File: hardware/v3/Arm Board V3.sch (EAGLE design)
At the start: 83 parts, among them CN1 1X4-BIG, IC1 L6208D, IC10 74LVC1G125DCK, IC2 L6208D, IC3 L6208D, IC4 LMV358IDGKR, IC5 NCP1117ST33T3G -3V3, IC6 ATMEGA16U2-MU, Q2 BC847BSMD, T1 FDN340P, T2 FDN340P, T3 FDN340P, U2 ST3485EBDR, U3 ATSAM3X8EA-AU, Y1 12MHz KX-7 20pF, Y2 32.768Khz, Y4 12MHz KX-7 20pF

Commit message: XBEE
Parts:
- added U$1: XBEE-1B2, SparkFun-RF:XBEE-1B2

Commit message: stuff
Expanded the board
Binded EA pin to PWMs
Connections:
- net PWM5: now also IC2.EN_B
- net PWM6: now also IC2.EN_A
- net PWM7: now also IC3.EN_A
- net PWM8: now also IC1.EN_A
- net PWM9: now also IC1.EN_B
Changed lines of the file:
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@@
+</segment>
+</net>
+<net name="PWM9" class="0">
+<segment>
+<pinref part="IC1" gate="G$1" pin="EN_B"/>
+<wire x1="43.18" y1="17.78" x2="45.72" y2="17.78" width="0.1524" layer="91"/>
+<label x="45.72" y="17.78" size="1.778" layer="95"/>
+</segment>
+</net>
+<net name="PWM8" class="0">
+<segment>
+<pinref part="IC1" gate="G$1" pin="EN_A"/>
+<wire x1="43.18" y1="40.64" x2="45.72" y2="40.64" width="0.1524" layer="91"/>
+<label x="45.72" y="40.64" size="1.778" layer="95"/>
+</segment>
+</net>
+<net name="PWM6" class="0">
+<segment>
+<pinref part="IC2" gate="G$1" pin="EN_A"/>
+<wire x1="106.68" y1="40.64" x2="109.22" y2="40.64" width="0.1524" layer="91"/>
+<label x="109.22" y="40.64" size="1.778" layer="95"/>
+</segment>
+</net>
+<net name="PWM5" class="0">
+<segment>
+<pinref part="IC2" gate="G$1" pin="EN_B"/>
+<wire x1="106.68" y1="17.78" x2="109.22" y2="17.78" width="0.1524" layer="91"/>
+<label x="109.22" y="17.78" size="1.778" layer="95"/>
+</segment>
+</net>
+<net name="PWM7" class="0">
+<segment>
+<pinref part="IC3" gate="G$1" pin="EN_A"/>
+<wire x1="175.26" y1="40.64" x2="177.8" y2="40.64" width="0.1524" layer="91"/>
+<label x="177.8" y="40.64" size="1.778" layer="95"/>
 </segment>
 </net>

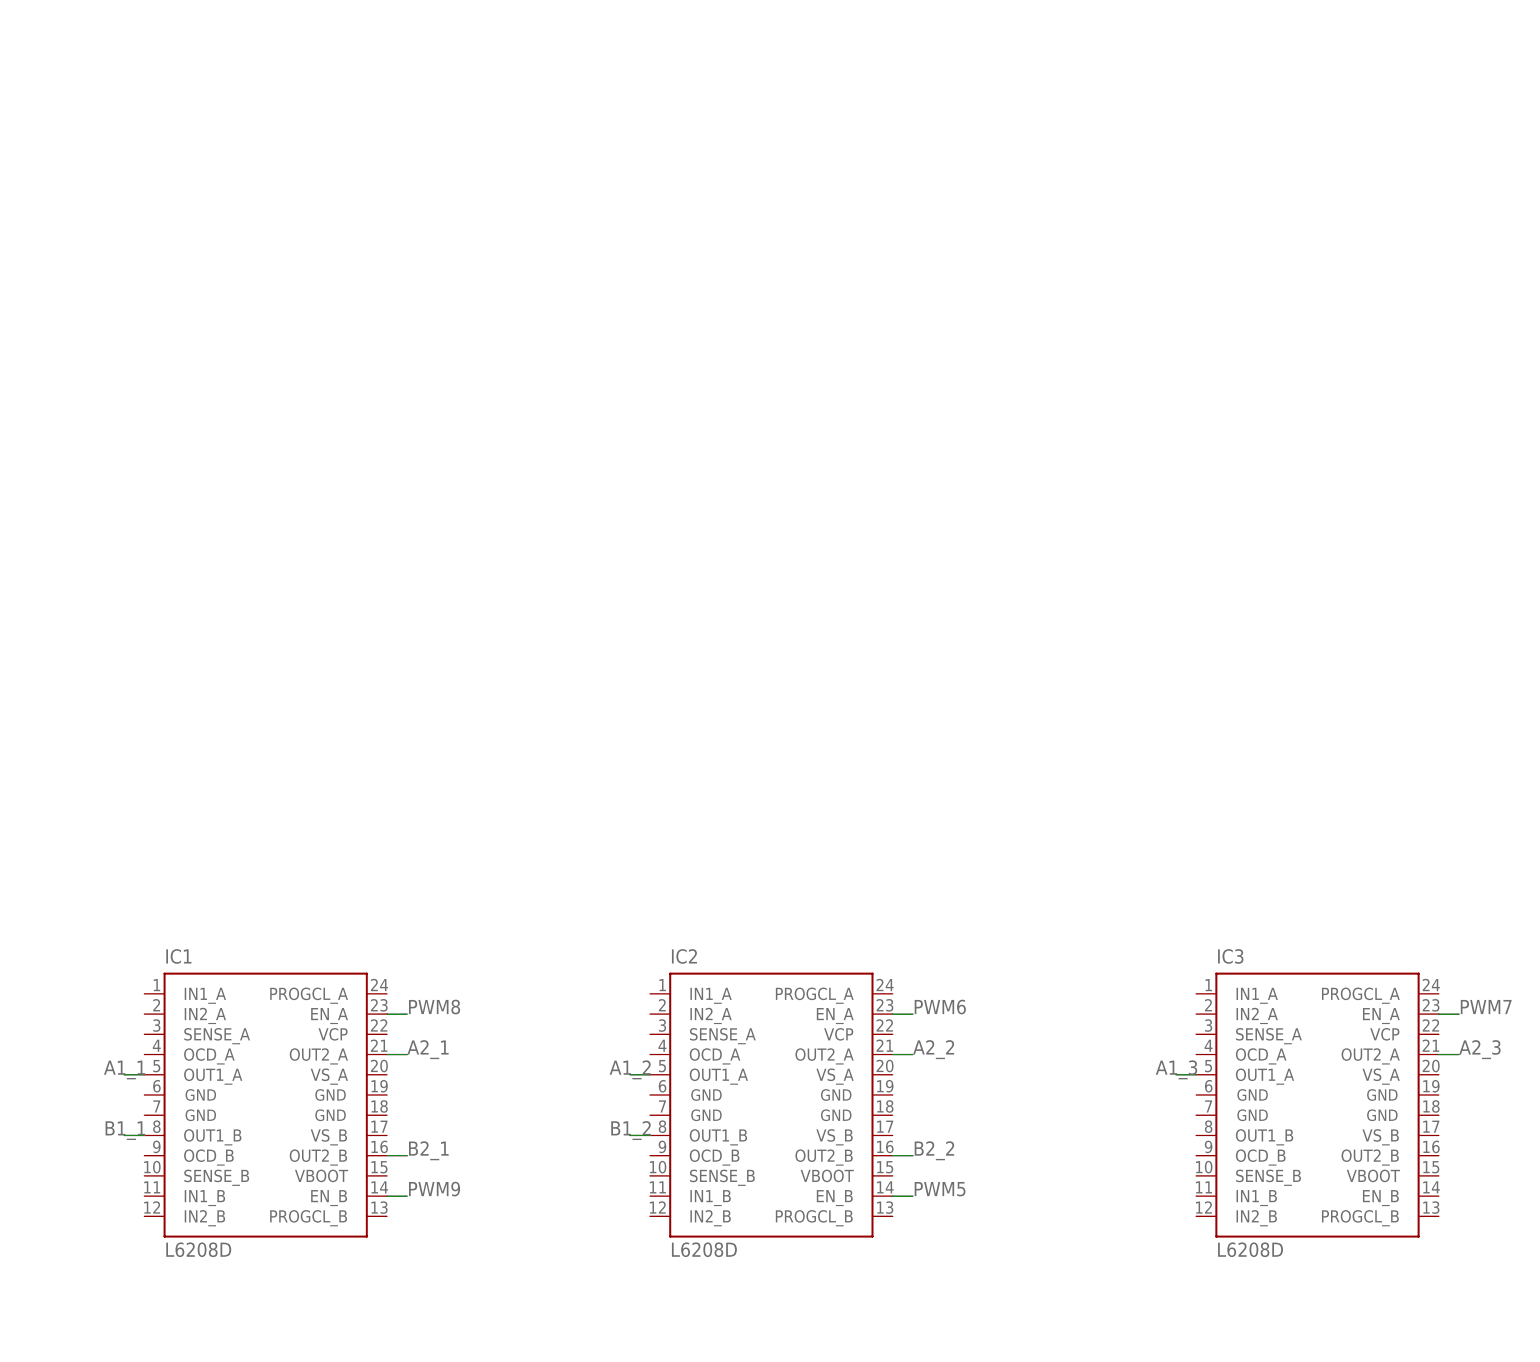
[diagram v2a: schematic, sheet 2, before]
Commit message: Connected motor controllers and Dynamixel
Bunch of stuff in the schematic
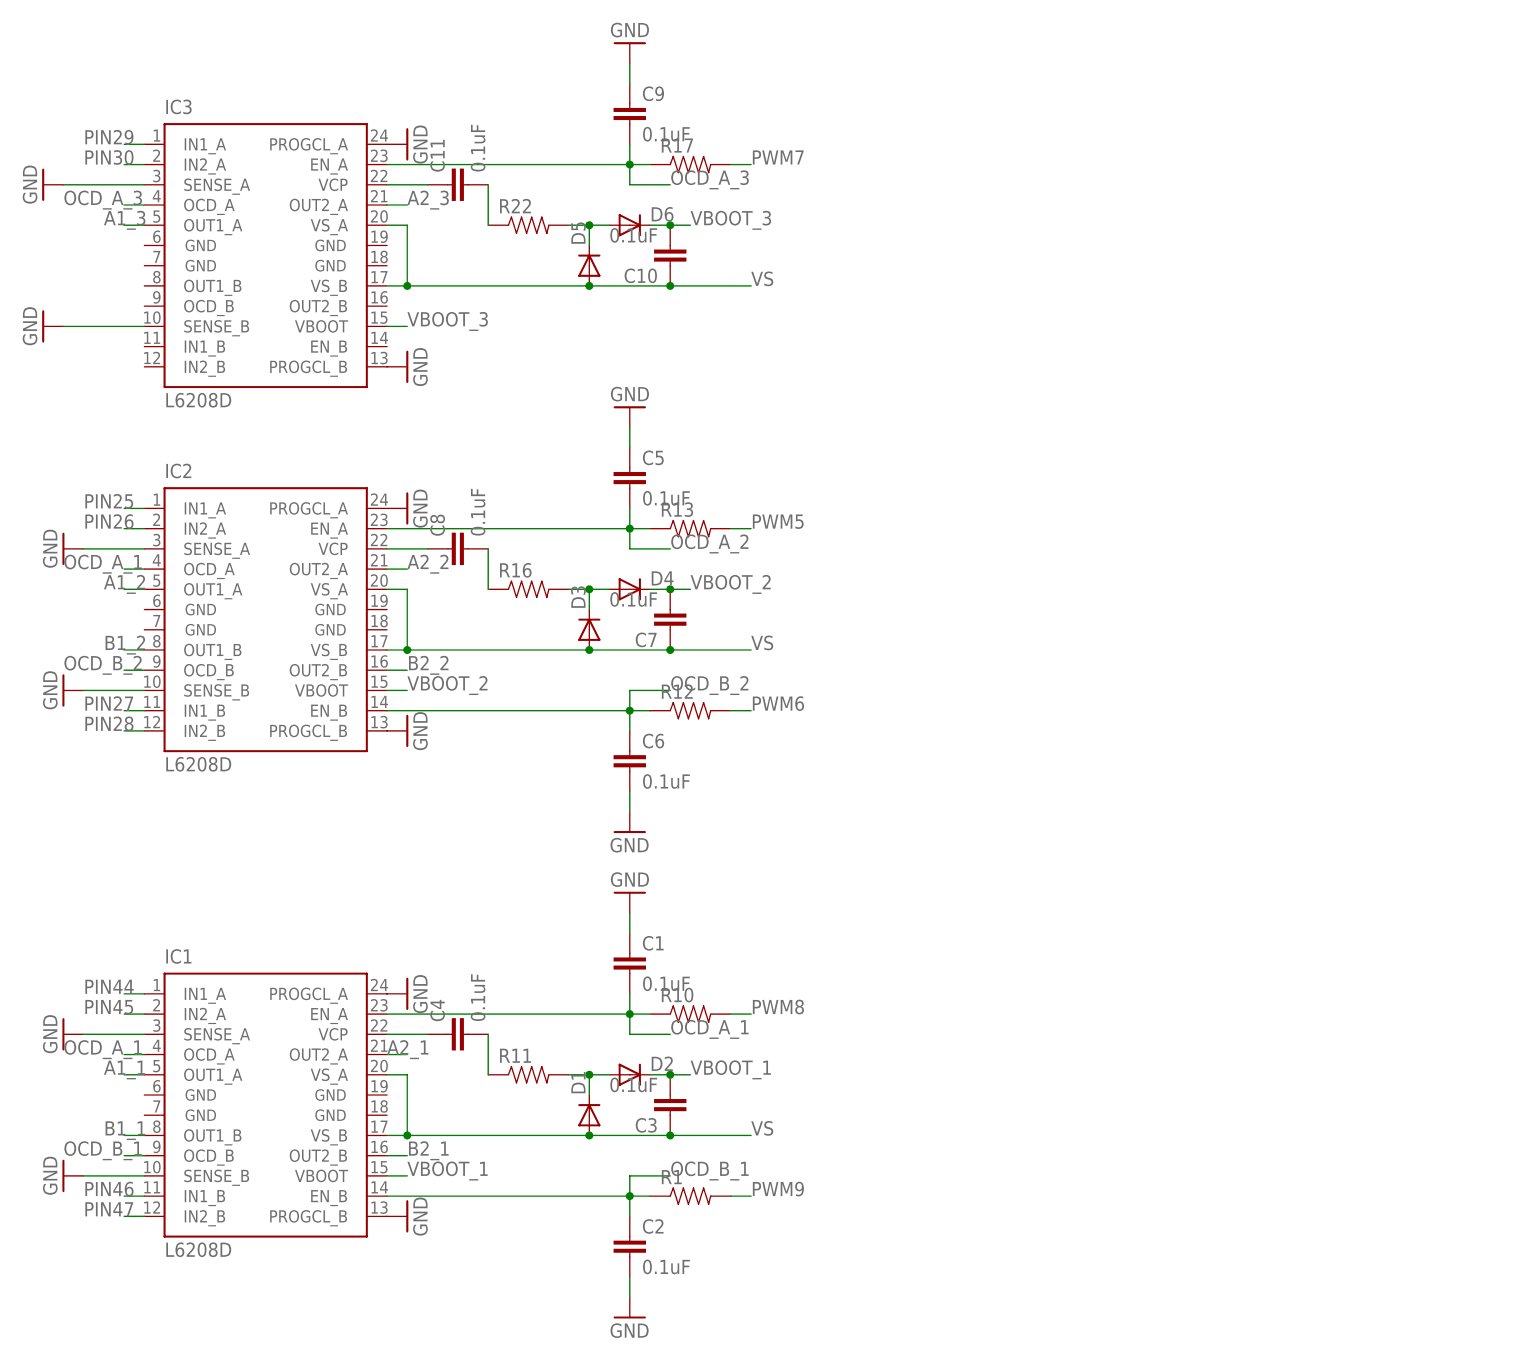
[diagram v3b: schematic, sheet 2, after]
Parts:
- removed C29: 10u, rcl:CPOL-EUSMCB
- removed C30: 100n, SmartPrj:C-EUC0402
- removed IC5: NCP1117ST33T3G -3V3, linear:MC33269ST-3.3T3
- added C1, C2, C5, C6, C9: 0.1uF, SparkFun-Capacitors:0.1UF-25V(+80/-20%)(0603)
- added C10, C11, C3, C4, C7, C8: 0.1uF, SparkFun-Capacitors:0.1UF-25V-5%(0603)
- added D1, D2, D3, D4, D5, D6: (no value), SparkFun-DiscreteSemi:DIODE1N4148
- added R1, R10, R11, R12, R13, R16, R17, R22: (no value), SparkFun-Passives:RESISTOR0805-RES
- added R24: 220, SparkFun-Passives:RESISTOR0805-RES
- U2: value ST3485EBDR -> MAX3468CSA; device ST Microelctronics_By_element14_Batch_1:ST3485EBDR -> maxim:MAX3468CSA
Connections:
- new net +12V: CN1.2
- new net DD+: CN1.3, R24.2, U2.B
- new net DD-: CN1.4, R24.1, U2.A
- new net N$10: C8.2, R16.1
- new net N$13: C4.1, IC1.VCP
- new net N$15: C4.2, R11.1
- new net N$16: C8.1, IC2.VCP
- new net N$17: D5.C, D6.A, R22.2
- new net N$18: C11.2, R22.1
- new net N$19: C11.1, IC3.VCP
- new net N$8: D3.C, D4.A, R16.2
- new net N$9: D1.C, D2.A, R11.2
- new net OCD_A_1: C1.2, IC1.EN_A, IC1.OCD_A, IC2.OCD_A, R10.1
- new net OCD_A_2: C5.2, IC2.EN_A, R13.1
- new net OCD_A_3: C9.2, IC3.EN_A, IC3.OCD_A, R17.1
- new net OCD_B_1: C2.1, IC1.EN_B, IC1.OCD_B, R1.1
- new net OCD_B_2: C6.1, IC2.EN_B, IC2.OCD_B, R12.1
- new net VBOOT_1: C3.2, D2.C, IC1.VBOOT
- new net VBOOT_2: C7.2, D4.C, IC2.VBOOT
- new net VBOOT_3: C10.2, D6.C, IC3.VBOOT
- new net VS: C10.1, C3.1, C7.1, D1.A, D3.A, D5.A, IC1.VS_A, IC1.VS_B, IC2.VS_A, IC2.VS_B, IC3.VS_A, IC3.VS_B
- net +3V3: no longer C29.+, IC5.OUT, IC5.OUT@1
- net +5V: now also U2.VCC; no longer C30.2, IC4P.V+, IC5.IN
- net GND: now also C1.1, C2.2, C5.1, C6.2, C9.1, CN1.1, IC1.PROGCL_A, IC1.PROGCL_B, IC1.SENSE_A, IC1.SENSE_B, IC2.PROGCL_A, IC2.PROGCL_B, IC2.SENSE_A, IC2.SENSE_B, IC3.PROGCL_A, IC3.PROGCL_B, IC3.SENSE_A, IC3.SENSE_B, U2.GND; no longer C29.-, C30.1, IC4P.V-, IC5.GND/ADJ
- net PIN23: now also U2.DE, U2.RE/
- net PIN25: now also IC2.IN1_A
- net PIN26: now also IC2.IN2_A
- net PIN27: now also IC2.IN1_B
- net PIN28: now also IC2.IN2_B
- net PIN29: now also IC3.IN1_A
- net PIN30: now also IC3.IN2_A
- net PIN44: now also IC1.IN1_A
- net PIN45: now also IC1.IN2_A
- net PIN46: now also IC1.IN1_B
- net PIN47: now also IC1.IN2_B
- net PWM5: now also R13.2; no longer IC2.EN_B
- net PWM6: now also R12.2; no longer IC2.EN_A
- net PWM7: now also R17.2; no longer IC3.EN_A
- net PWM8: now also R10.2; no longer IC1.EN_A
- net PWM9: now also R1.2; no longer IC1.EN_B
- net RXD1: now also U2.RO
- net TXD1: now also U2.DI
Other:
- moved on the sheet: CN1, IC2, IC3

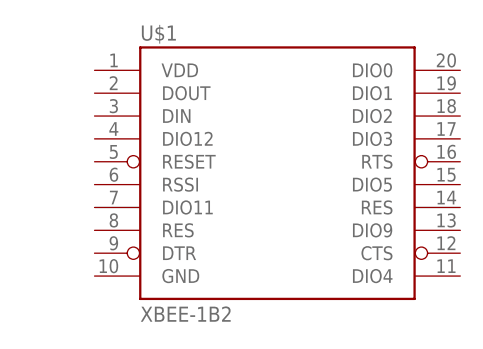
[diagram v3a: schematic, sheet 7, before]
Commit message: Added Xbee connections to schematic
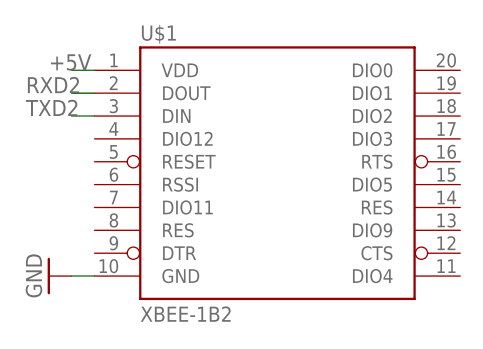
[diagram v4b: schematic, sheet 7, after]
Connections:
- net +5V: now also U$1.VDD
- net GND: now also U$1.GND
- net RXD2: now also U$1.DOUT
- net TXD2: now also U$1.DIN
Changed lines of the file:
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@@
 <part name="GND54" library="SparkFun-Aesthetics" deviceset="GND" device=""/>
 <part name="R24" library="SparkFun-Passives" deviceset="RESISTOR" device="0805-RES" value="220"/>
+<part name="GND16" library="SparkFun-Aesthetics" deviceset="GND" device=""/>
 </parts>
 <sheets>
@@
 <instances>
 <instance part="U$1" gate="G$1" x="43.18" y="35.56"/>
+<instance part="GND16" gate="1" x="17.78" y="22.86" rot="R270"/>
 </instances>
 <busses>
 </busses>
 <nets>
+<net name="+5V" class="0">
+<segment>
+<pinref part="U$1" gate="G$1" pin="VDD"/>
+<wire x1="22.86" y1="45.72" x2="20.32" y2="45.72" width="0.1524" layer="91"/>
+<label x="17.78" y="45.72" size="1.778" layer="95"/>
+</segment>
+</net>
+<net name="TXD2" class="0">
+<segment>
+<pinref part="U$1" gate="G$1" pin="DIN"/>
+<wire x1="22.86" y1="40.64" x2="20.32" y2="40.64" width="0.1524" layer="91"/>
+<label x="15.24" y="40.64" size="1.778" layer="95"/>
+</segment>
+</net>
+<net name="GND" class="0">
+<segment>
+<pinref part="U$1" gate="G$1" pin="GND"/>
+<wire x1="22.86" y1="22.86" x2="20.32" y2="22.86" width="0.1524" layer="91"/>
+<pinref part="GND16" gate="1" pin="GND"/>
+</segment>
+</net>
+<net name="RXD2" class="0">
+<segment>
+<pinref part="U$1" gate="G$1" pin="DOUT"/>
+<wire x1="22.86" y1="43.18" x2="20.32" y2="43.18" width="0.1524" layer="91"/>
+<label x="15.24" y="43.18" size="1.778" layer="95"/>
+</segment>
+</net>
 </nets>
 </sheet>

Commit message: Added Launchpad to Board
This included adding it to the schematic, widening the board, and
placing components.
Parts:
- removed BR1: NM, bibaja:J0402
- removed C19, C28, C31, C32, C34, C36, C37: 100n, SmartPrj:C-EUC0402
- removed C20, C26: 10n, SmartPrj:C-EUC0402
- removed C21, C22, C25, C39, C40: 22p, SmartPrj:C-EUC0402
- removed C23, C24: 22pF_NM, SmartPrj:C-EUC0402
- removed C27, C33, C35: 10u, rcl:CPOL-EUSMCB
- removed C38: 1u, SmartPrj:C-EUC0402
- removed ERASE: (no value), SmartPrj:MYSMD_PB157
- removed F1, F2: MF-MSMF050-2 500mA, rcl:L-EUL1812
- removed IC10: 74LVC1G125DCK, 74xx-little-us:74LVC1G125DCK
- removed IC4: LMV358IDGKR, linear:LMV358MMX
- removed IC6: ATMEGA16U2-MU, SmartPrj:ATMEGA16U2-MU
- removed JP7: M025MM, SparkFun-Connectors:M025MM
- removed JR1: 0R, SmartPrj:R-EU_R0402
- removed L, RX, RX1, TX, TX1: YELLOW, led:LEDCHIP-LED0805
- removed L3, L5: MH2029-300Y, wuerth-elektronik:WE-CBF_0805
- removed ON: GREEN, led:LEDCHIP-LED0805
- removed Q2: BC847BSMD, transistor-npn:BC847BSMD
- removed R10, R11, R12, R13, R16, R17, R22: (no value), SparkFun-Passives:RESISTOR0805-RES
- removed R14, R15, R21: 1K, SmartPrj:R-EU_R0402
- removed R18: 10K, SmartPrj:R-EU_R0402
- removed R19, R20: 22R, SmartPrj:R-EU_R0402
- removed R23: 1K, Resistenze:0140_1K_0402
- removed R24: 220, SparkFun-Passives:RESISTOR0805-RES
- removed RESET: TS42, SmartPrj:TS42
- removed RN3: 1k, resistor-dil:4R-NCAY16
- removed RN4: 100K, resistor-dil:4R-NCAT16
- removed T1, T2, T3: FDN340P, zetex:PMOSSOT23
- removed U2: MAX3468CSA, maxim:MAX3468CSA
- removed U3: ATSAM3X8EA-AU, SmartPrj:ATSAM3X/AAU
- removed U4: (no value), SparkFun-Connectors:USB-ABCONN-11794
- removed Y1, Y4: 12MHz KX-7 20pF, SmartPrj:CRYSTAL-3.2-2.5
- removed Y2: 32.768Khz, Arduino_Wifi_shield_v018_tG:RESONATOR_EPSON_FC_145
- removed Z1, Z2, Z3, Z4, Z5: CG0603MLC-05E, varistor:VARISTORCN0603
- added JP6: M025MM, SparkFun-Connectors:M025MM
- added U$2: XBEE-1B2, SparkFun-RF:XBEE-1B2
- C11, C4, C7, C8: device SparkFun-Capacitors:0.1UF-25V-5%(0603) -> SparkFun-Capacitors:0.1UF-25V(+80/-20%)(0603)
- C2, C5, C6, C9: device SparkFun-Capacitors:0.1UF-25V(+80/-20%)(0603) -> SparkFun-Capacitors:0.1UF-25V-5%(0603)
- R2: value 10K -> (none); device SmartPrj:R-EU_R0402 -> SparkFun-Passives:RESISTOR0805-RES
- R3: value 1K -> (none); device SmartPrj:R-EU_R0402 -> SparkFun-Passives:RESISTOR0805-RES
- R4: value 100K -> (none); device SmartPrj:R-EU_R0402 -> SparkFun-Passives:RESISTOR0805-RES
- R5, R6: value 39R 1% -> (none); device SmartPrj:R-EU_R0402 -> SparkFun-Passives:RESISTOR0805-RES
- R7: value 6k8 1% -> (none); device SmartPrj:R-EU_R0603 -> SparkFun-Passives:RESISTOR0805-RES
- R8: value 0R_NM -> (none); device SmartPrj:R-EU_R0402 -> SparkFun-Passives:RESISTOR0805-RES
- R9: value 1M_NM -> 220; device SmartPrj:R-EU_R0402 -> SparkFun-Passives:RESISTOR0805-RES
- U$1: value XBEE-1B2 -> STELLARIS-LAUNCHPADSTELLARIS-LAUNCHPAD-XL; device SparkFun-RF:XBEE-1B2 -> StellarisLaunchPad_Fred:STELLARIS-LAUNCHPADSTELLARIS-LAUNCHPAD-XL
- U1: value (none) -> MAX3468CSA; device SparkFun-Connectors:USB-ABCONN-11794 -> maxim:MAX3468CSA
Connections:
- removed net +3V3: BR1.2, C20.2, C37.1, ERASE.1, IC10P.VCC, IC4B.-IN, JR1.1, R4.2, RN3A.2, RN3B.2, RN3D.2, T3.S, U3.VDDBU, U3.VDDIN, U3.VDDIO1, U3.VDDIO2, U3.VDDIO3, U3.VDDIO4
- removed net 16U2-TX: IC10A.I, IC6.(TXD1/INT3)PD3
- removed net AD0: U3.PA16
- removed net AD1: U3.PA24
- removed net AD10: U3.PB19
- removed net AD11(TXD3): U3.PB20
- removed net AD14(RXD3): U3.PB21
- removed net AD2: U3.PA23
- removed net AD3: U3.PA22
- removed net AD4: U3.PA6
- removed net AD5: U3.PA4
- removed net AD6: U3.PA3
- removed net AD7: U3.PA2
- removed net AD8: U3.PB17
- removed net AD9: U3.PB18
- removed net AREF: BR1.1
- removed net AVREF: C19.2, L3.2, U3.ADVREF
- removed net AVREFL: BR1.C, C34.2, JR1.2, L3.1
- removed net BD+: R20.2, U4.D+, Z4.2
- removed net BD-: R19.2, U4.D-, Z3.2
- removed net CANRX0: U3.PA1
- removed net CANTX0: U3.PA0
- removed net CANTX1/IO: U3.PB14
- removed net CMP: C31.2, IC4B.+IN, Q2.C, RN4C.1, RN4D.1
- removed net D+: R6.1, U1.D+, U3.DHSDP, Z1.1
- removed net D-: R5.1, U1.D-, U3.DHSDM, Z2.1
- removed net DAC0(CANRX1): U3.PB15
- removed net DAC1: U3.PB16
- removed net DTR: IC6.(CTS/HWB/AIN6/TO/INT7)PD7, R18.1
- removed net EEXTINT: U3.PA5
- removed net EMDC: U3.PB8
- removed net EMDIO: U3.PB9
- removed net ERASE_CMD: IC6.(OC1A/PCINT8)PC6, T3.G
- removed net ERASE_S: ERASE.2, T3.D, U3.PC0
- removed net ERXD0: U3.PB5
- removed net ERXD1: U3.PB6
- removed net ERX_DV: U3.PB4
- removed net ERX_ER: U3.PB7
- removed net ETXD0: U3.PB2
- removed net ETXD1: U3.PB3
- removed net ETX_CLK: U3.PB0
- removed net ETX_EN: U3.PB1
- removed net GATE_CMD: IC4B.OUT, T1.G
- removed net JTAG_TCK: U3.PB28
- removed net JTAG_TDI: U3.PB29
- removed net JTAG_TDO: U3.PB30
- removed net JTAG_TMS: U3.PB31
- removed net L13: IC4A.-IN, IC4A.OUT, RN3C.2
- removed net MASTER-RESET: C20.1, R23.2, RESET.3, RESET.4, U3.NRSTB
- removed net MISO: U3.PA25
- removed net MOSI: U3.PA26
- removed net N$1: IC6.(PCINT10)PC4, R21.1
- removed net N$11: R5.2, U3.DFSDM
- removed net N$12: R6.2, U3.DFSDP
- removed net N$14: R14.2, TX1.A
- removed net N$2: L.A, RN3C.1
- removed net N$3: ON.A, RN3D.1
- removed net N$4: R15.2, RX1.A
- removed net N$5: R8.2, U3.TST
- removed net N$54: RN3A.1, RX.A
- removed net N$55: RN3B.1, TX.A
- removed net N$6: Q2.B, R3.2, RN4A.2
- removed net N$7: R4.1, U3.FWUP
- removed net PIN22: U3.PB26
- removed net PIN24: U3.PA15
- removed net PIN31: U3.PA7
- removed net PIN32: U3.PD10
- removed net PIN33: U3.PC1
- removed net PIN34: U3.PC2
- removed net PIN35: U3.PC3
- removed net PIN36: U3.PC4
- removed net PIN37: U3.PC5
- removed net PIN38: U3.PC6
- removed net PIN39: U3.PC7
- removed net PIN40: U3.PC8
- removed net PIN41: U3.PC9
- removed net PIN42: U3.PA19
- removed net PIN43: U3.PA20
- removed net PIN48: U3.PC15
- removed net PIN49: U3.PC14
- removed net PIN50: U3.PC13
- removed net PIN51: U3.PC12
- removed net PWM11: U3.PD7
- removed net PWM12: U3.PD8
- removed net PWM13: IC4A.+IN, U3.PB27
- removed net PWM2: U3.PB25
- removed net PWM3: U3.PC28
- removed net RD+: IC6.D+, R20.1
- removed net RD-: IC6.D-, R19.1
- removed net RESET_CMD: IC6.(INT4/ICP1/CLK0)PC7, R23.1
- removed net RX: IC10A.O, U3.PA8
- removed net RXD0: U3.PD5
- removed net RXL: RX.C, U3.PC30
- removed net RXL-U2: IC6.(INT5/AIN3)PD4, RX1.C
- removed net SCL0-3: U3.PB13
- removed net SCL1: U3.PA18
- removed net SDA0-3: U3.PB12
- removed net SDA1: U3.PA17
- removed net SPCK: U3.PA27
- removed net SS0/PWM10: U3.PA28, U3.PC29
- removed net SS1/PWM4: U3.PA29, U3.PC26
- removed net SS3: U3.PB23
- removed net TX: IC6.(RXD1/AIN1/INT2)PD2, U3.PA9
- removed net TXD0: U3.PD4
- removed net TXL: TX.C, U3.PA21
- removed net TXL-U2: IC6.(XCK/AIN4/PCINT12)PD5, TX1.C
- removed net UOTGID: U1.USBID, U3.PB11, Z5.2
- removed net UOTGVBOF: R3.1, U3.PB10
- removed net USBVCC: C27.+, C35.+, F1.1, R2.2, R21.2, T1.D
- removed net USBVCCU2: C28.1, F2.1, IC6.UVCC, T2.D
- removed net VBG: C25.1, R7.2, U3.VBG
- removed net VDDANA: U3.VDDANA
- removed net VDDOUT: L5.1, U3.VDDCORE1, U3.VDDCORE2, U3.VDDCORE3, U3.VDDCORE4, U3.VDDCORE5, U3.VDDOUT
- removed net VDDOUTMI: U3.VDDUTMI
- removed net VDDPLL: C32.2, C33.+, L5.2, U3.VDDPLL
- removed net VUCAP: C38.1, IC6.UCAP
- removed net XIN: C22.1, U3.XIN, Y1.C1
- removed net XIN32: C24.1, U3.XIN32, Y2.2
- removed net XOUT: C21.1, U3.XOUT, Y1.C2
- removed net XOUT32: C23.1, U3.XOUT32, Y2.1
- removed net XT1: C39.1, IC6.XTAL1, R9.1, Y4.C1
- removed net XT2: C40.1, IC6.XTAL2(PC0), R9.2, Y4.C2
- removed net XUSB: C26.1, F1.2, U1.VBUS, U3.VBUS
- removed net XVCC: F2.2, U4.VBUS
- net +5V: now also U$2.VDD, U1.VCC; no longer C36.1, IC6.AVCC, IC6.VCC, R14.1, R15.1, T1.S, T2.S, U$1.VDD, U2.VCC
- net A1_1: now also IC3.OUT1_A, JP2.1; no longer IC1.OUT1_A, JP1.1
- net A1_2: now also JP4.1; no longer JP3.1
- net A1_3: now also IC1.OUT1_A, JP6.2; no longer IC3.OUT1_A, JP5.2
- net A2_1: now also IC3.OUT2_A, JP2.2; no longer IC1.OUT2_A, JP1.2
- net A2_2: now also JP4.2; no longer JP3.2
- net A2_3: now also IC1.OUT2_A, JP6.1; no longer IC3.OUT2_A, JP5.1
- net B1_1: now also IC3.OUT1_B, JP3.1; no longer IC1.OUT1_B, JP2.1
- net B1_2: now also JP5.1; no longer JP4.1
- net B2_1: now also IC3.OUT2_B, JP3.2; no longer IC1.OUT2_B, JP2.2
- net B2_2: now also JP5.2; no longer JP4.2
- net DD+: now also R9.2, U1.B; no longer R24.2, U2.B
- net DD-: now also R9.1, U1.A; no longer R24.1, U2.A
- net GND: now also C11.2, C4.1, C7.2, C8.1, JP1.2, U$2.GND; no longer C19.1, C2.2, C21.2, C22.2, C23.2, C24.2, C25.2, C26.2, C27.-, C28.2, C31.1, C32.1, C33.-, C34.1, C35.-, C36.2, C37.2, C38.2, C39.2, C40.2, C5.1, C6.2, C9.1, IC10A.OE, IC10P.GND, IC6.GND, IC6.PAD, IC6.UGND, JP7.2, L.C, ON.C, Q2.E, R18.2, R2.1, R7.1, R8.1, RESET.1, RESET.2, RN4A.1, RN4B.1, RN4B.2, RN4D.2, T2.G, U$1.GND, U2.GND, U3.GND1, U3.GND2, U3.GND3, U3.GND4, U3.GNDANA, U3.GNDBU, U3.GNDPLL, U3.GNDUTMI, U3.JTAGSEL, U4.GND, Y1.GND@1, Y1.GND@2, Y4.GND@1, Y4.GND@2, Z1.2, Z2.2, Z3.1, Z4.1, Z5.1
- net N$10: now also C5.2, R4.1; no longer C8.2, R16.1
- net N$13: now also C9.1, IC3.VCP; no longer C4.1, IC1.VCP
- net N$15: now also C9.2, R7.1; no longer C4.2, R11.1
- net N$16: now also C5.1; no longer C8.1
- net N$17: now also D1.A, D2.C, R2.2; no longer D5.C, D6.A, R22.2
- net N$18: now also C2.2, R2.1; no longer C11.2, R22.1
- net N$19: now also C2.1, IC1.VCP; no longer C11.1, IC3.VCP
- net N$8: now also D3.A, D4.C, R4.2; no longer D3.C, D4.A, R16.2
- net N$9: now also D5.A, D6.C, R7.2; no longer D1.C, D2.A, R11.2
- net OCD_A_1: now also C8.2, IC3.EN_A, IC3.OCD_A, R6.1; no longer C1.2, IC1.EN_A, IC1.OCD_A, R10.1
- net OCD_A_2: now also C4.2, R3.1; no longer C5.2, R13.1
- net OCD_A_3: now also C1.2, IC1.EN_A, IC1.OCD_A, R1.1; no longer C9.2, IC3.EN_A, IC3.OCD_A, R17.1
- net OCD_B_1: now also C11.1, IC3.EN_B, IC3.OCD_B, R8.1; no longer C2.1, IC1.EN_B, IC1.OCD_B, R1.1
- net OCD_B_2: now also C7.1, R5.1; no longer C6.1, R12.1
- net PIN23: now also U1.DE, U1.RE/; no longer U2.DE, U2.RE/, U3.PA14
- net PIN25: no longer U3.PD0
- net PIN26: no longer U3.PD1
- net PIN27: no longer U3.PD2
- net PIN28: no longer U3.PD3
- net PIN29: now also IC1.IN1_A; no longer IC3.IN1_A, U3.PD6
- net PIN30: now also IC1.IN2_A; no longer IC3.IN2_A, U3.PD9
- net PIN44: now also IC3.IN1_A; no longer IC1.IN1_A, U3.PC19
- net PIN45: now also IC3.IN2_A; no longer IC1.IN2_A, U3.PC18
- net PIN46: now also IC3.IN1_B; no longer IC1.IN1_B, U3.PC17
- net PIN47: now also IC3.IN2_B; no longer IC1.IN2_B, U3.PC16
- net PWM5: now also R3.2; no longer R13.2, U3.PC25
- net PWM6: now also R5.2; no longer R12.2, U3.PC24
- net PWM7: now also R1.2; no longer R17.2, U3.PC23
- net PWM8: now also R6.2; no longer R10.2, U3.PC22
- net PWM9: now also R8.2; no longer R1.2, U3.PC21
- net RXD1: now also U1.RO; no longer U2.RO, U3.PA12
- net RXD2: now also U$2.DOUT; no longer U$1.DOUT, U3.PA10
- net TXD1: now also U1.DI; no longer U2.DI, U3.PA13
- net TXD2: now also U$2.DIN; no longer U$1.DIN, U3.PA11
- net VBOOT_1: now also C10.2, D5.C, IC3.VBOOT; no longer C3.2, D2.C, IC1.VBOOT
- net VBOOT_2: now also C6.2, D3.C; no longer C7.2, D4.C
- net VBOOT_3: now also C3.2, D1.C, IC1.VBOOT; no longer C10.2, D6.C, IC3.VBOOT
- net VIN: now also JP1.1; no longer JP7.1, RN4C.2
- net VS: now also C6.1, D2.A, D4.A, D6.A; no longer C7.1, D1.A, D3.A, D5.A
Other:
- note removed: "(ETH)"
- note removed: "(SD)"
- note removed: "(board powered from external power supply)"
- note removed: "0: The UOTGVBOF output signal is in its default mode (active high)"
- note removed: "1: The UOTGVBOF output signal is inverted (active low)"
- note removed: "CONFIG 5V"
- note removed: "CONNECT"
- note removed: "ERASE"
- note removed: "Forces OFF the power supply to USB port"
- note removed: "JTAG"
- note removed: "N.C."
- note removed: "N.C. - internal pullup"
- note removed: "USB AB"
- note removed: "USB boot En"
- note removed: "VBUSPO: VBus Polarity Off"
- note removed: "when the USB port is in HOST mode"
